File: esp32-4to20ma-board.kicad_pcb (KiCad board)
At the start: 2 copper layers, 40 x 61 mm, 59 parts, among them J1 USB-C Receptacle, J2 4-20mA Loop, Q1 BCP53-16, Q2 MMBT5401, Q3 AO3401A, Q4 2N7002, SW1 RESET, SW2 BOOT, U1 ESP32-S3-WROOM-1U-N4, U3 INA226AIDGSR, U4 AP2112K-3.3, U5 MT3608

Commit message: docs: describe the firmware as a published remote package
Co-Authored-By: Claude Opus 5 <noreply@anthropic.com>
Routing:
- net +3V3: track 0.00 -> 107.5 mm, vias 0 -> 3
- net +5V: track 0.00 -> 59.6 mm, vias 0 -> 3
- net /USB_N: track 0.00 -> 43.8 mm, vias 0 -> 2
- net /I2C_SCL: track 0.00 -> 41.3 mm, vias 0 -> 2
- net GND: track 0.00 -> 39.8 mm, vias 0 -> 40
- net /USB_P: track 0.00 -> 39.6 mm
- net /I2C_SDA: track 0.00 -> 38.7 mm, vias 0 -> 2
- net /EN: track 0.00 -> 32.2 mm, vias 0 -> 2
- net /LOOP_V: track 0.00 -> 27.2 mm, vias 0 -> 1
- net /LOOP_RTN: track 0.00 -> 23.3 mm
- net +24V: track 0.00 -> 21.1 mm
- net /IO0: track 0.00 -> 17.9 mm, vias 0 -> 2
- net /MT_EN: track 0.00 -> 14.2 mm
- net /LOOP_SNS: track 0.00 -> 13.4 mm
- net /VIN_SW: track 0.00 -> 13.4 mm
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- added copper zone on B.Cu, net /LOOP_C
- added copper zone on F.Cu, net /LOOP_C
- added copper zone on B.Cu, net GND
- added copper zone on F.Cu, net GND

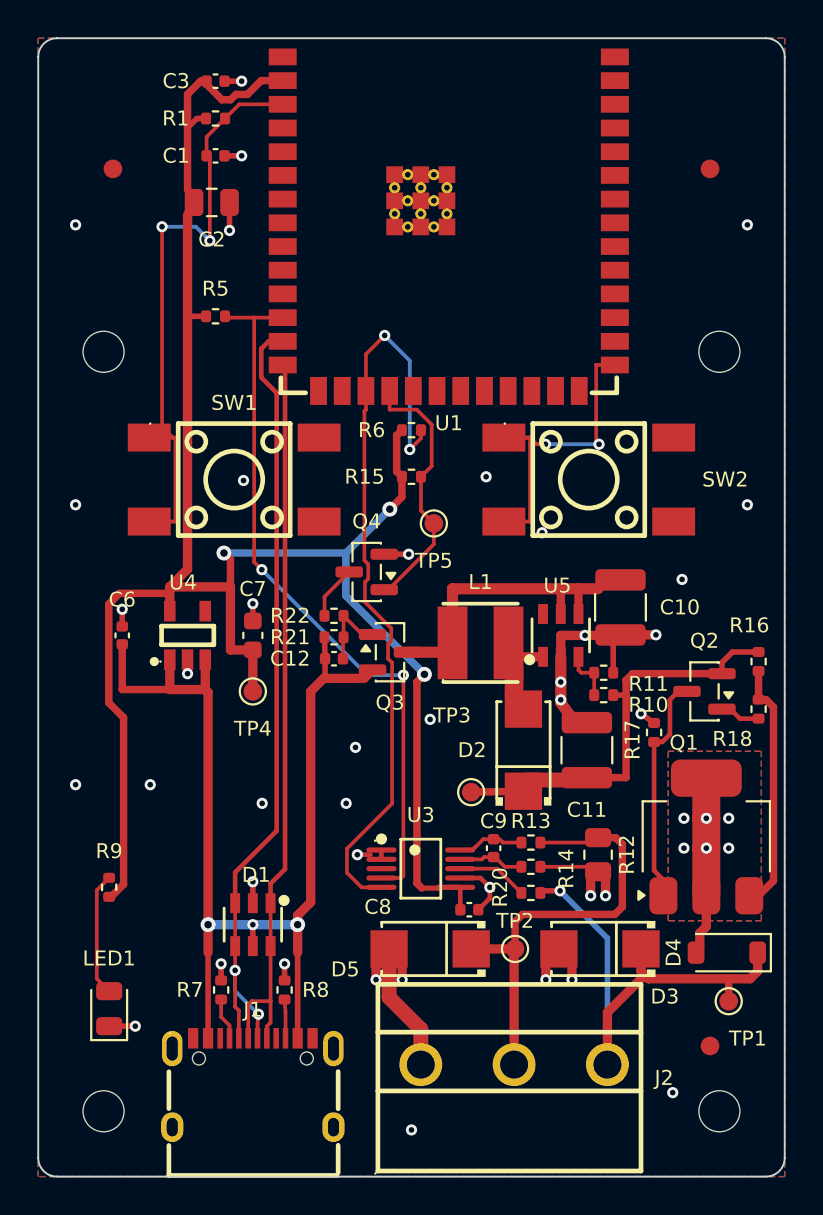
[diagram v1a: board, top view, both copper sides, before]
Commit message: Rev G: board routed, schematic regrouped, JLCPCB package
Routing
- route_board.py on routelib.py: the MT3608 loop (datasheet Figure 3), the
  INA226 Kelvin taps (Figure 30), the USB-C entry and pair, the power trunks,
  the 24 V loop, Q1's copper on both layers, every ground via and both pours
  are scripted; ten signal nets are Freerouting 2.4.1's, stored in
  routing/autoroute.json and replayed, so the board rebuilds byte-identically
  without Java. 0 unconnected, DRC unchanged at 4 + 5, parity clean, bottom
  ground in one piece, no via in any pad.
- Placement changes routing asked for: D1 turned 180 and moved up, R7/R8 into
  the lanes beside the connector, R10/R11 beside U5, C9 up 0.1 mm, R6/R15
  swapped so each pull-up sits under its own pin.
- setup_fab.py keeps the project's existing board rules (0.5 mm copper to edge).

Schematic
- Twelve hand-typed boxes became seven content-derived blocks, one per
  circuit, notes inside their block; nothing touches an outline (schlib's new
  outline check: ~100 faults on the old sheet, 0 now). Netlist unchanged:
  28 nets, ERC 0 errors. INA226 address pins share one ground port.
- Nine manufacturer names corrected against LCSC (every LCSC number and MPN
  was already right).

Fabrication
- build_package.py -> fab/: gerbers zip, 34-line BOM, 47-row CPL, order notes,
  behind a DRC gate. Standard PCBA is required (the ESP32-S3-WROOM-1U-N4 is
  "Standard Only" at JLCPCB). CPL rotations derived by jlc_compare.py from
  JLCPCB's own footprints: Q1-Q4 +180, everything else at zero; unverified
  until seen in their placement preview.

Housekeeping: the autorouter's work folder (scratch, with local paths in its
logs) was committed by mistake earlier; it is removed and ignored.

Co-Authored-By: Claude Fable 5.1 <noreply@anthropic.com>
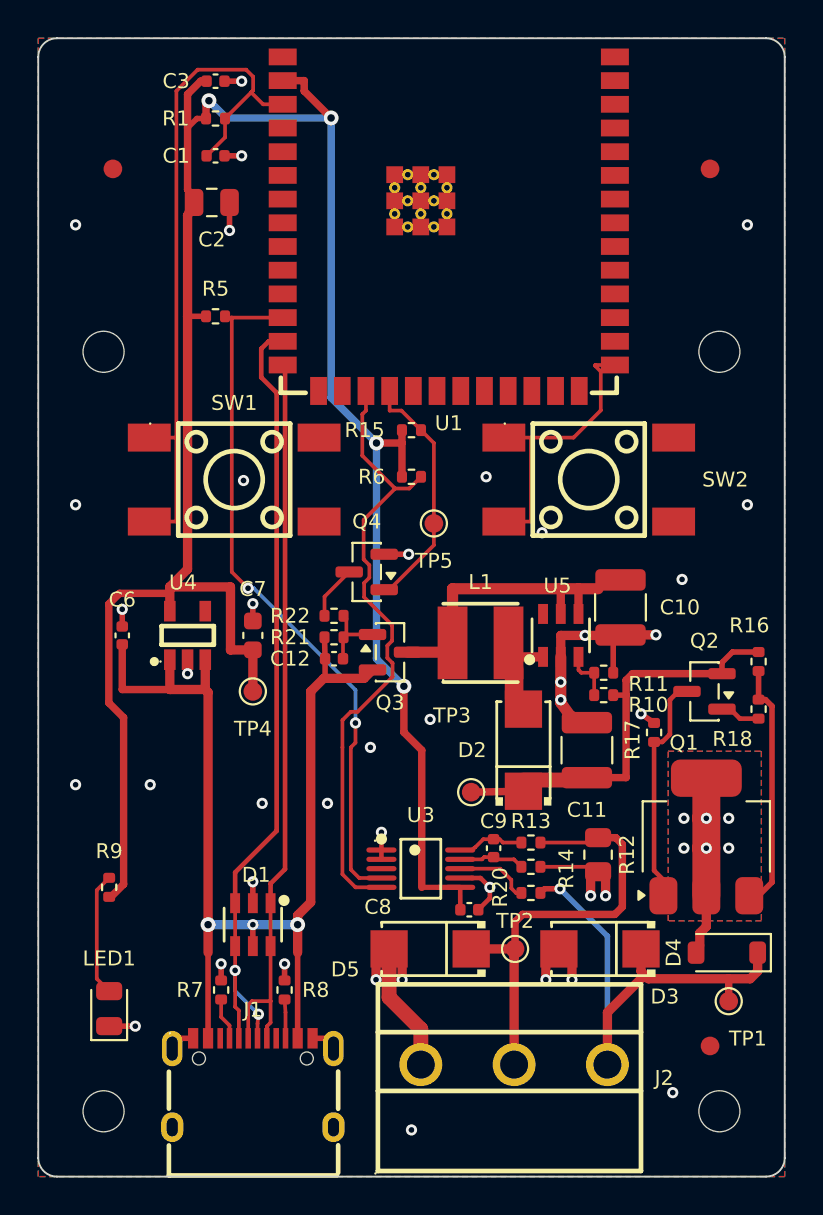
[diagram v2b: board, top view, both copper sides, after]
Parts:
- moved R15 2.50 mm to (120.0, 71.0)
- moved R6 2.50 mm to (120.0, 73.5)
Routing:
- net +3V3: track 107.5 -> 124.7 mm, vias 3 -> 4
- net /I2C_SCL: track 41.3 -> 33.8 mm, vias 2 -> 0
- net /EN: track 32.2 -> 37.9 mm, vias 2 -> 0
- net /IO0: track 17.9 -> 15.4 mm, vias 2 -> 0
- net GND: track 39.8 -> 41.7 mm
- net /I2C_SDA: track 38.7 -> 37.6 mm
- net /MT_EN: track 14.2 -> 13.3 mm
